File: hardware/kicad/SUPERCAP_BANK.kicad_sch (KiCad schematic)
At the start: 0 parts

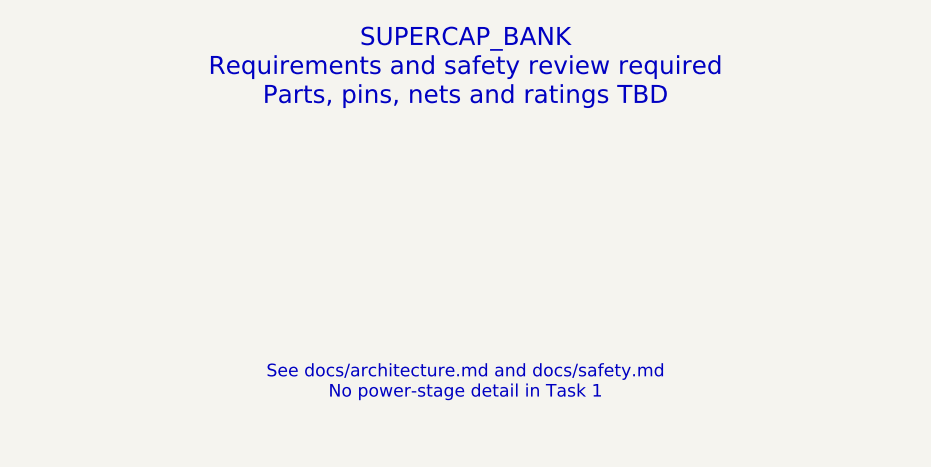
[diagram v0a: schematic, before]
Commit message: hardware: update existing KiCad architecture and add precharge sheet
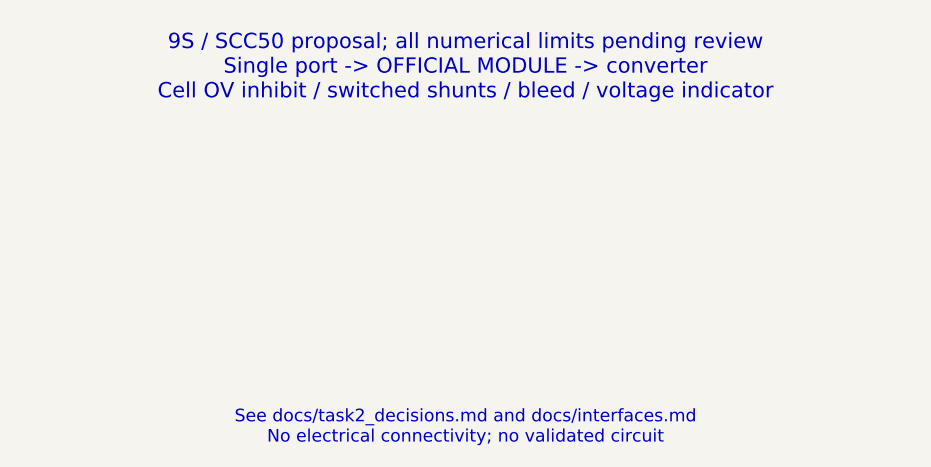
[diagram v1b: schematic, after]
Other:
- note added: "9S / SCC50 proposal; all numerical limits pending review Single port -> OFFICIAL MODULE -> converter Cell OV inhibit / switched shunts / bleed / voltage indicator"
- note added: "See docs/task2_decisions.md and docs/interfaces.md No electrical connectivity; no validated circuit"
- note removed: "SUPERCAP_BANK Requirements and safety review required Parts, pins, nets and ratings TBD"
- note removed: "See docs/architecture.md and docs/safety.md No power-stage detail in Task 1"
- title: SUPERCAP_BANK - Placeholder -> SUPERCAP_BANK - Task 2 Proposal

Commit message: hardware: implement prototype Rev A electrical schematic
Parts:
- added C62, C63, C64, C65, C66, C67, C68, C69, C70: 100nF /50V X7R, Capacitor_SMD:C_0805_2012Metric, symbol RevA:C
- added C71, C72, C73, C74, C75: 100nF / 16V X7R, Capacitor_SMD:C_0805_2012Metric, symbol RevA:C
- added C76: 1uF /50V X7R, Capacitor_SMD:C_0805_2012Metric, symbol RevA:C
- added C77: 470nF /50V X7R, Capacitor_SMD:C_0805_2012Metric, symbol RevA:C
- added C78, C79, C80: 1uF /16V, Capacitor_SMD:C_0805_2012Metric, symbol RevA:C
- added D25: SS110 flyback candidate / release delay MUST VERI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, Diode_SMD:D_SMA, symbol RevA:D
- added F2: ATOF 58V 15A candidate / bidirectional DC interru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, symbol RevA:FUSE
- added J15: 9S bank power -> official module external boundary, symbol RevA:J2
- added J16: CAP_ISO external actuator+feedback, symbol RevA:J4
- added J17: Protected 9S taps / SOURCE-SIDE resistors mandato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, symbol RevA:J10
- added K6: CAP_ISO external NO contact / AEV14012 candidate, symbol RevA:CONTACT
- added Q20: CSD18540Q5B, Package_SON:VSONP-8-1EP_5x6_P1.27mm, symbol RevA:CSD18540Q5B
- added Q21: BC857B, Package_TO_SOT_SMD:SOT-23, symbol RevA:Q_PNP
- added Q22: BC847B, Package_TO_SOT_SMD:SOT-23, symbol RevA:Q_NPN
- added Q23: BC847B preregulator / voltage thermal MUST VERIFY, Package_TO_SOT_SMD:SOT-23, symbol RevA:Q_NPN
- added R122, R123, R124, R128, R139, R140, R141, R142, R143, R145, R146, R150, R151: 10k, Resistor_SMD:R_0805_2012Metric, symbol RevA:R
- added R125: 4.7k, Resistor_SMD:R_0805_2012Metric, symbol RevA:R
- added R126: 100k, Resistor_SMD:R_0805_2012Metric, symbol RevA:R
- added R127: 47R, Resistor_SMD:R_0805_2012Metric, symbol RevA:R
- added R129, R130, R131, R132, R133, R134, R135, R136, R137, R138: 1k /1W tap protection / no bypass, Resistor_SMD:R_2512_6332Metric, symbol RevA:R
- added R144: 100R, Resistor_SMD:R_0805_2012Metric, symbol RevA:R
- added R147, R148, R149: 10k TS commissioning option, Resistor_SMD:R_0805_2012Metric, symbol RevA:R
- added U21: BQ7694204PFBR, Package_QFP:TQFP-48_7x7mm_P0.5mm, symbol RevA:BQ7694204PFBR
- added U22: SN74LV1T34DBVR, Package_TO_SOT_SMD:SOT-23-5, symbol RevA:SN74LV1T34DBVR
- added U23: TPS3839K33DBZR, Package_TO_SOT_SMD:SOT-23, symbol RevA:TPS3839K33DBZR
- added U24: SN74LVC2G08DCUR, Package_SO:VSSOP-8_2.3x2mm_P0.5mm, symbol RevA:SN74LVC2G08DCUR
- added U25, U26: TMUX1511PWR, Package_SO:TSSOP-14_4.4x5mm_P0.65mm, symbol RevA:TMUX1511PWR
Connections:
- new net ACTUATOR_12V: D25.1 (K), J16.1 (P1), K6.3 (COIL_P), Q21.2 (E), R123.2 (B)
- new net BANK_FUSED: F2.2 (B), K6.1 (COM)
- new net BANK_P_RAW: F2.1 (A), J15.1 (P1), J17.10 (P10), R138.1 (A), R144.1 (A), R145.1 (A), R146.1 (A)
- new net CAP_ISOLATED: K6.2 (NO)
- new net CAP_ISO_COIL_GATE: Q20.2 (G_DS4), R122.1 (A), R127.2 (B)
- new net CAP_ISO_COIL_M: D25.2 (A), J16.2 (P2), K6.4 (COIL_M), Q20.3 (D_DS5_6_7_8)
- new net CAP_ISO_DRIVE: R125.1 (A)
- new net CAP_ISO_FB: J16.3 (P3), R128.1 (A)
- new net CAP_ISO_NPN_C: Q22.3 (C), R124.2 (B)
- new net CAP_ISO_NPN_C_BASE: Q22.1 (B), R125.2 (B), R126.1 (A)
- new net CAP_ISO_PNP_B: Q21.1 (B), R123.1 (A), R124.1 (A)
- new net CAP_ISO_PNP_C: Q21.3 (C), R127.1 (A)
- new net CELL0_FILTER: C62.2 (B), R129.2 (B), U21.16 (VC0)
- new net CELL1_FILTER: C62.1 (A), C63.2 (B), R130.2 (B), U21.15 (VC1)
- new net CELL1_RAW: J17.2 (P2), R130.1 (A)
- new net CELL2_FILTER: C63.1 (A), C64.2 (B), R131.2 (B), U21.14 (VC2)
- new net CELL2_RAW: J17.3 (P3), R131.1 (A)
- new net CELL3_FILTER: C64.1 (A), C65.2 (B), R132.2 (B), U21.13 (VC3)
- new net CELL3_RAW: J17.4 (P4), R132.1 (A)
- new net CELL4_FILTER: C65.1 (A), C66.2 (B), R133.2 (B), U21.12 (VC4)
- new net CELL4_RAW: J17.5 (P5), R133.1 (A)
- new net CELL5_FILTER: C66.1 (A), C67.2 (B), R134.2 (B), U21.10 (VC5)
- new net CELL5_RAW: J17.6 (P6), R134.1 (A)
- new net CELL6_FILTER: C67.1 (A), C68.2 (B), R135.2 (B), U21.8 (VC6)
- new net CELL6_RAW: J17.7 (P7), R135.1 (A)
- new net CELL7_FILTER: C68.1 (A), C69.2 (B), R136.2 (B), U21.6 (VC7)
- new net CELL7_RAW: J17.8 (P8), R136.1 (A)
- new net CELL8_FILTER: C69.1 (A), C70.2 (B), R137.2 (B), U21.2 (VC9), U21.4 (VC8)
- new net CELL8_RAW: J17.9 (P9), R137.1 (A)
- new net CELL9_FILTER: C70.1 (A), R138.2 (B), U21.48 (VC10)
- new net GND: C71.2 (B), C72.2 (B), C73.2 (B), C74.2 (B), C75.2 (B), C76.2 (B), C78.2 (B), C79.2 (B), C80.2 (B), J15.2 (P2), J16.4 (P4), J17.1 (P1), Q20.1 (S_DS1_2_3), Q22.2 (E), R122.2 (B), R126.2 (B), R129.1 (A), R139.2 (B), R142.2 (B), R143.2 (B), R147.2 (B), R148.2 (B), R149.2 (B), R150.2 (B), R151.2 (B), U21.17 (VSS), U21.18 (SRP), U21.20 (SRN), U21.30 (DFETOFF), U21.33 (RST_SHUT), U22.3 (GND), U23.1 (GND), U24.4 (GND), U24.5 (A2), U24.6 (B2), U25.7 (GND), U26.12 (S4), U26.5 (S2), U26.7 (GND), U26.9 (S3)
- new net MON_ALERT: R140.1 (A), U21.25 (ALERT), U26.2 (S1)
- new net MON_ALERT_HOST: U26.3 (D1)
- new net MON_BAT: C76.1 (A), C77.2 (B), Q23.3 (C), R144.2 (B), U21.47 (BAT)
- new net MON_BREG: Q23.1 (B), U21.37 (BREG)
- new net MON_COMM_PERMIT: U24.7 (Y1), U25.1 (SEL1), U25.10 (SEL3), U25.13 (SEL4), U25.4 (SEL2), U26.1 (SEL1), U26.10 (SEL3), U26.13 (SEL4), U26.4 (SEL2)
- new net MON_CP: C77.1 (A), U21.46 (CP1)
- new net MON_CS: R141.1 (A), U21.29 (CS_N), U25.8 (D3)
- new net MON_CS_HOST: U25.9 (S3)
- new net MON_DCHG: R150.1 (A), U21.31 (DCHG)
- new net MON_DDSG: R151.1 (A), U21.32 (DDSG)
- new net MON_LD: R146.2 (B), U21.41 (LD)
- new net MON_MISO: R139.1 (A), U21.27 (MISO), U22.2 (A)
- new net MON_MISO_HOST: U25.11 (D4)
- new net MON_MISO_SHIFTED: U22.4 (Y), U25.12 (S4)
- new net MON_MOSI: R143.1 (A), U21.28 (MOSI), U25.6 (D2)
- new net MON_MOSI_HOST: U25.5 (S2)
- new net MON_PACK: R145.2 (B), U21.42 (PACK)
- new net MON_POWER_OK: U23.2 (RESET_N), U24.2 (B1)
- new net MON_REG1: C71.1 (A), C72.1 (A), C79.1 (A), R140.2 (B), R141.2 (B), U21.35 (REG1), U22.5 (VCC), U23.3 (VDD)
- new net MON_REG18: C80.1 (A), U21.24 (REG18)
- new net MON_REGIN: C78.1 (A), Q23.2 (E), U21.36 (REGIN)
- new net MON_SCLK: R142.1 (A), U21.26 (SCLK), U25.3 (D1)
- new net MON_SCLK_HOST: U25.2 (S1)
- new net MON_TS1: R147.1 (A), U21.21 (TS1)
- new net MON_TS2: R148.1 (A), U21.22 (TS2)
- new net MON_TS3: R149.1 (A), U21.23 (TS3)
- new net RAIL_OK: U24.1 (A1)
- new net V3V3: C73.1 (A), C74.1 (A), C75.1 (A), R128.2 (B), U24.8 (VCC), U25.14 (VDD), U26.14 (VDD)
- no-connect marks 0 -> 19
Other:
- note added: "BQ battery-ground SPI is not galvanically isolated; partial-power/backfeed review still mandatory."
- note added: "BQ7694204 SPI/CRC +3.3V REG1 variant. 9S mask: cells1..8 +cell10, VC9 tied to VC8, unused cell9 disabled."
- note added: "DCHG/DDSG configured ACTIVE-HIGH permission, pull-down, protection mapping/readback+power-cycle test mandatory."
- note added: "Internal switched passive balance limited by1k input R; charge must taper/inhibit if balancing cannot keep up."
- note added: "Open-wire current/settling plus input R must be validated; harness source protection before connector is mandatory."
- note added: "Standalone COV/CUV/protection need verified provisioning; defaults for Li-ion are NOT supercap settings."
- note added: "TMUX SPI/ALERT disconnect if either MCU or REG1 power missing; LV1T34 handles initial1.8V MISO level."
- note removed: "9S / SCC50 proposal; all numerical limits pending review Single port -> OFFICIAL MODULE -> converter Cell OV inhibit / switched shunts / bleed / voltage indicator"
- note removed: "See docs/task2_decisions.md and docs/interfaces.md No electrical connectivity; no validated circuit"
- title: SUPERCAP_BANK - Task 2 Proposal -> SUPERCAP_BANK / Prototype Rev A draft

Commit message: hardware: refine Rev A protection and passive selections
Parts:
- removed C62, C63, C64, C65, C66, C67, C68, C69, C70: 100nF /50V X7R, Capacitor_SMD:C_0805_2012Metric, symbol RevA:C
- removed C71: 100nF / 16V X7R, Capacitor_SMD:C_0805_2012Metric, symbol RevA:C
- removed D25: SS110 flyback candidate / release delay MUST VERI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, Diode_SMD:D_SMA, symbol RevA:D
- removed F2: ATOF 58V 15A candidate / bidirectional DC interru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, symbol RevA:FUSE
- removed J15: 9S bank power -> official module external boundary, symbol RevA:J2
- removed J16: CAP_ISO external actuator+feedback, symbol RevA:J4
- removed J17: Protected 9S taps / SOURCE-SIDE resistors mandato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, symbol RevA:J10
- removed K6: CAP_ISO external NO contact / AEV14012 candidate, symbol RevA:CONTACT
- removed Q20: CSD18540Q5B, Package_SON:VSONP-8-1EP_5x6_P1.27mm, symbol RevA:CSD18540Q5B
- removed Q21: BC857B, Package_TO_SOT_SMD:SOT-23, symbol RevA:Q_PNP
- removed Q22: BC847B, Package_TO_SOT_SMD:SOT-23, symbol RevA:Q_NPN
- removed Q23: BC847B preregulator / voltage thermal MUST VERIFY, Package_TO_SOT_SMD:SOT-23, symbol RevA:Q_NPN
- removed U21: BQ7694204PFBR, Package_QFP:TQFP-48_7x7mm_P0.5mm, symbol RevA:BQ7694204PFBR
- removed U22: SN74LV1T34DBVR, Package_TO_SOT_SMD:SOT-23-5, symbol RevA:SN74LV1T34DBVR
- removed U23: TPS3839K33DBZR, Package_TO_SOT_SMD:SOT-23, symbol RevA:TPS3839K33DBZR
- removed U24: SN74LVC2G08DCUR, Package_SO:VSSOP-8_2.3x2mm_P0.5mm, symbol RevA:SN74LVC2G08DCUR
- added C81, C82, C83, C84, C85, C86, C87, C88, C89: 100nF /50V X7R, Capacitor_SMD:C_0805_2012Metric, symbol RevA:C
- added C90, C91, C92, C93, C94: 100nF / 16V X7R, Capacitor_SMD:C_0805_2012Metric, symbol RevA:C
- added C95: 1uF /50V X7R, Capacitor_SMD:C_0805_2012Metric, symbol RevA:C
- added C96, C97, C98: 1uF /16V, Capacitor_SMD:C_0805_2012Metric, symbol RevA:C
- added D23: SMBJ18CA bidirectional coil suppression / release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, Diode_SMD:D_SMB, symbol RevA:D
- added F3: 0997015.WXN / MINI997 58V15A / external 0FHM0002Z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, symbol RevA:FUSE
- added J12: 9S bank power -> official module external boundary, symbol RevA:J2
- added J13: CAP_ISO actuator+reserved diagnostic / no intrins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, symbol RevA:J4
- added J14: Protected 9S taps / source resistors at electrode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, symbol RevA:J10
- added K4: CAP_ISO external NO contact / AEV14012 bench sele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, symbol RevA:CONTACT
- added Q16: CSD18540Q5B, Package_SON:VSONP-8-1EP_5x6_P1.27mm, symbol RevA:CSD18540Q5B
- added Q17: BC857B, Package_TO_SOT_SMD:SOT-23, symbol RevA:Q_PNP
- added Q18: BC847B, Package_TO_SOT_SMD:SOT-23, symbol RevA:Q_NPN
- added Q19: BC847B preregulator / voltage thermal MUST VERIFY, Package_TO_SOT_SMD:SOT-23, symbol RevA:Q_NPN
- added R116, R117, R118, R155, R156: 10k, Resistor_SMD:R_0805_2012Metric, symbol RevA:R
- added R119: 4.7k, Resistor_SMD:R_0805_2012Metric, symbol RevA:R
- added R120: 100k, Resistor_SMD:R_0805_2012Metric, symbol RevA:R
- added R121: 47R, Resistor_SMD:R_0805_2012Metric, symbol RevA:R
- added R152, R153, R154: 10k TS commissioning option, Resistor_SMD:R_0805_2012Metric, symbol RevA:R
- added U27: SN74LV1T34DBVR, Package_TO_SOT_SMD:SOT-23-5, symbol RevA:SN74LV1T34DBVR
- added U28: TPS3839K33DBZR, Package_TO_SOT_SMD:SOT-23, symbol RevA:TPS3839K33DBZR
- added U29: SN74LVC2G08DCUR, Package_SO:VSSOP-8_2.3x2mm_P0.5mm, symbol RevA:SN74LVC2G08DCUR
- added U30, U31: TMUX1511PWR, Package_SO:TSSOP-14_4.4x5mm_P0.65mm, symbol RevA:TMUX1511PWR
- C72, C73, C74, C75: value 100nF / 16V X7R -> 50F /2.7V SCCV40B506SRB / external cell; footprint Capacitor_SMD:C_0805_2012Metric -> (none); MPN (none) -> SCCV40B506SRB
- C76: value 1uF /50V X7R -> 50F /2.7V SCCV40B506SRB / external cell; footprint Capacitor_SMD:C_0805_2012Metric -> (none); MPN (none) -> SCCV40B506SRB
- C77: value 470nF /50V X7R -> 50F /2.7V SCCV40B506SRB / external cell; footprint Capacitor_SMD:C_0805_2012Metric -> (none); MPN (none) -> SCCV40B506SRB
- C78, C79, C80: value 1uF /16V -> 50F /2.7V SCCV40B506SRB / external cell; footprint Capacitor_SMD:C_0805_2012Metric -> (none); MPN (none) -> SCCV40B506SRB
- R122, R143, R145, R146, R150, R151: MPN (none) -> CRCW080510K0FKEA
- R123, R124, R128: value 10k -> 1k /1W EXTERNAL cell-terminal tap resistor; footprint Resistor_SMD:R_0805_2012Metric -> (none); MPN (none) -> CRCW25121K00FKEG
- R125: value 4.7k -> 1k /1W EXTERNAL cell-terminal tap resistor; footprint Resistor_SMD:R_0805_2012Metric -> (none); MPN (none) -> CRCW25121K00FKEG
- R126: value 100k -> 1k /1W EXTERNAL cell-terminal tap resistor; footprint Resistor_SMD:R_0805_2012Metric -> (none); MPN (none) -> CRCW25121K00FKEG
- R127: value 47R -> 1k /1W EXTERNAL cell-terminal tap resistor; footprint Resistor_SMD:R_0805_2012Metric -> (none); MPN (none) -> CRCW25121K00FKEG
- R129, R130, R131, R132: value 1k /1W tap protection / no bypass -> 1k /1W EXTERNAL cell-terminal tap resistor; footprint Resistor_SMD:R_2512_6332Metric -> (none); MPN (none) -> CRCW25121K00FKEG
- R133, R134, R135, R136, R137, R138: MPN (none) -> CRCW25121K00FKEG
- R139, R140, R141, R142: value 10k -> 1k /1W tap protection / no bypass; footprint Resistor_SMD:R_0805_2012Metric -> Resistor_SMD:R_2512_6332Metric; MPN (none) -> CRCW25121K00FKEG
- R144: value 100R -> 10k; MPN (none) -> CRCW080510K0FKEA
- R147: value 10k TS commissioning option -> 10k; MPN (none) -> CRCW080510K0FKEA
- R148: value 10k TS commissioning option -> 100R; MPN (none) -> CRCW0805100RFKEA
- R149: value 10k TS commissioning option -> 0R; MPN (none) -> CRCW08050000Z0EA
- U25: value TMUX1511PWR -> Blue Sea6006 / external manual bank disconnect;not a fault breaker; footprint Package_SO:TSSOP-14_4.4x5mm_P0.65mm -> (none); symbol RevA:TMUX1511PWR -> RevA:DISCONNECT; MPN (none) -> 6006
- U26: value TMUX1511PWR -> BQ7694204PFBR; footprint Package_SO:TSSOP-14_4.4x5mm_P0.65mm -> Package_QFP:TQFP-48_7x7mm_P0.5mm; symbol RevA:TMUX1511PWR -> RevA:BQ7694204PFBR; MPN (none) -> BQ7694204PFBR
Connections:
- net ACTUATOR_12V: now also D23.1 (K), J13.1 (P1), K4.3 (COIL_P), Q17.2 (E), R117.2 (B); no longer R123.2 (B)
- net BANK_FUSED: now also F3.2 (B), K4.1 (COM)
- net BANK_P_RAW: now also C80.1 (A), R132.1 (A), R148.1 (A), R150.1 (A), R151.1 (A), U25.1 (COM), J12.1 (P1); no longer R138.1 (A), R144.1 (A), R145.1 (A), R146.1 (A)
- net CAP_ISOLATED: now also K4.2 (NO)
- net CAP_ISO_COIL_GATE: now also Q16.2 (G_DS4), R116.1 (A), R121.2 (B); no longer R122.1 (A), R127.2 (B)
- net CAP_ISO_COIL_M: now also D23.2 (A), J13.2 (P2), K4.4 (COIL_M), Q16.3 (D_DS5_6_7_8)
- net CAP_ISO_DRIVE: now also R119.1 (A); no longer R125.1 (A)
- net CAP_ISO_FB: now also R122.1 (A), J13.3 (P3); no longer R128.1 (A)
- net CAP_ISO_NPN_C: now also Q18.3 (C), R118.2 (B); no longer R124.2 (B)
- net CAP_ISO_NPN_C_BASE: now also Q18.1 (B), R119.2 (B), R120.1 (A); no longer R125.2 (B), R126.1 (A)
- net CAP_ISO_PNP_B: now also Q17.1 (B), R117.1 (A), R118.1 (A); no longer R123.1 (A), R124.1 (A)
- net CAP_ISO_PNP_C: now also Q17.3 (C), R121.1 (A); no longer R127.1 (A)
- net CELL0_FILTER: now also R133.2 (B), U26.16 (VC0), C81.2 (B); no longer R129.2 (B)
- net CELL1_FILTER: now also R134.2 (B), U26.15 (VC1), C81.1 (A), C82.2 (B); no longer R130.2 (B)
- net CELL1_RAW: now also C72.1 (A), C73.2 (B), R124.1 (A); no longer R130.1 (A)
- net CELL2_FILTER: now also R135.2 (B), U26.14 (VC2), C82.1 (A), C83.2 (B); no longer R131.2 (B)
- net CELL2_RAW: now also C73.1 (A), C74.2 (B), R125.1 (A); no longer R131.1 (A)
- net CELL3_FILTER: now also R136.2 (B), U26.13 (VC3), C83.1 (A), C84.2 (B); no longer R132.2 (B)
- net CELL3_RAW: now also C74.1 (A), C75.2 (B), R126.1 (A); no longer R132.1 (A)
- net CELL4_FILTER: now also R137.2 (B), U26.12 (VC4), C84.1 (A), C85.2 (B); no longer R133.2 (B)
- net CELL4_RAW: now also C75.1 (A), C76.2 (B), R127.1 (A); no longer R133.1 (A)
- net CELL5_FILTER: now also R138.2 (B), U26.10 (VC5), C85.1 (A), C86.2 (B); no longer R134.2 (B)
- net CELL5_RAW: now also C76.1 (A), C77.2 (B), R128.1 (A); no longer R134.1 (A)
- net CELL6_FILTER: now also R139.2 (B), U26.8 (VC6), C86.1 (A), C87.2 (B); no longer R135.2 (B)
- net CELL6_RAW: now also C77.1 (A), C78.2 (B), R129.1 (A); no longer R135.1 (A)
- net CELL7_FILTER: now also R140.2 (B), U26.6 (VC7), C87.1 (A), C88.2 (B); no longer R136.2 (B)
- net CELL7_RAW: now also C78.1 (A), C79.2 (B), R130.1 (A); no longer R136.1 (A)
- net CELL8_FILTER: now also R141.2 (B), U26.2 (VC9), U26.4 (VC8), C88.1 (A), C89.2 (B); no longer R137.2 (B)
- net CELL8_RAW: now also C79.1 (A), C80.2 (B), R131.1 (A); no longer R137.1 (A)
- net CELL9_FILTER: now also R142.2 (B), U26.48 (VC10), C89.1 (A); no longer R138.2 (B)
- net GND: now also R123.1 (A), R146.2 (B), U26.17 (VSS), U26.18 (SRP), U26.20 (SRN), U26.30 (DFETOFF), U26.33 (RST_SHUT), C90.2 (B), C91.2 (B), C92.2 (B), C93.2 (B), C94.2 (B), C95.2 (B), C96.2 (B), C97.2 (B), C98.2 (B), J12.2 (P2), J13.4 (P4), Q16.1 (S_DS1_2_3), Q18.2 (E), R116.2 (B), R120.2 (B), R152.2 (B), R153.2 (B), R154.2 (B), R155.2 (B), R156.2 (B), U27.3 (GND), U28.1 (GND), U29.4 (GND), U29.5 (A2), U29.6 (B2), U30.7 (GND), U31.12 (S4), U31.5 (S2), U31.7 (GND), U31.9 (S3); no longer C73.2 (B), C74.2 (B), C75.2 (B), C76.2 (B), C78.2 (B), C79.2 (B), C80.2 (B), R126.2 (B), R129.1 (A), R139.2 (B), R142.2 (B), R148.2 (B), R149.2 (B), R150.2 (B), R151.2 (B), U25.7 (GND), U26.12 (S4), U26.5 (S2), U26.7 (GND), U26.9 (S3)
- net MON_ALERT: now also R144.1 (A), U26.25 (ALERT), U31.2 (S1); no longer R140.1 (A), U26.2 (S1)
- net MON_ALERT_HOST: now also U31.3 (D1); no longer U26.3 (D1)
- net MON_BAT: now also R148.2 (B), R149.2 (B), U26.47 (BAT), C95.1 (A), Q19.3 (C); no longer C76.1 (A), C77.2 (B), R144.2 (B)
- net MON_BREG: now also U26.37 (BREG), Q19.1 (B)
- net MON_COMM_PERMIT: now also U29.7 (Y1), U30.1 (SEL1), U30.10 (SEL3), U30.13 (SEL4), U30.4 (SEL2), U31.1 (SEL1), U31.10 (SEL3), U31.13 (SEL4), U31.4 (SEL2); no longer U25.1 (SEL1), U25.10 (SEL3), U25.13 (SEL4), U25.4 (SEL2), U26.1 (SEL1), U26.10 (SEL3), U26.13 (SEL4), U26.4 (SEL2)
- net MON_CP: now also R149.1 (A), U26.46 (CP1); no longer C77.1 (A)
- net MON_CS: now also R145.1 (A), U26.29 (CS_N), U30.8 (D3); no longer R141.1 (A), U25.8 (D3)
- net MON_CS_HOST: now also U30.9 (S3); no longer U25.9 (S3)
- net MON_DCHG: now also U26.31 (DCHG), R155.1 (A); no longer R150.1 (A)
- net MON_DDSG: now also U26.32 (DDSG), R156.1 (A); no longer R151.1 (A)
- net MON_LD: now also R151.2 (B), U26.41 (LD); no longer R146.2 (B)
- net MON_MISO: now also R143.1 (A), U26.27 (MISO), U27.2 (A); no longer R139.1 (A)
- net MON_MISO_HOST: now also U30.11 (D4); no longer U25.11 (D4)
- net MON_MISO_SHIFTED: now also U27.4 (Y), U30.12 (S4); no longer U25.12 (S4)
- net MON_MOSI: now also R147.1 (A), U26.28 (MOSI), U30.6 (D2); no longer R143.1 (A), U25.6 (D2)
- net MON_MOSI_HOST: now also U30.5 (S2); no longer U25.5 (S2)
- net MON_PACK: now also R150.2 (B), U26.42 (PACK); no longer R145.2 (B)
- net MON_POWER_OK: now also U28.2 (RESET_N), U29.2 (B1)
- net MON_REG1: now also R144.2 (B), R145.2 (B), U26.35 (REG1), C90.1 (A), C91.1 (A), C97.1 (A), U27.5 (VCC), U28.3 (VDD); no longer C72.1 (A), C79.1 (A), R140.2 (B), R141.2 (B)
- net MON_REG18: now also U26.24 (REG18), C98.1 (A); no longer C80.1 (A)
- net MON_REGIN: now also U26.36 (REGIN), C96.1 (A), Q19.2 (E); no longer C78.1 (A)
- net MON_SCLK: now also R146.1 (A), U26.26 (SCLK), U30.3 (D1); no longer R142.1 (A), U25.3 (D1)
- net MON_SCLK_HOST: now also U30.2 (S1); no longer U25.2 (S1)
- net MON_TS1: now also U26.21 (TS1), R152.1 (A); no longer R147.1 (A)
- net MON_TS2: now also U26.22 (TS2), R153.1 (A); no longer R148.1 (A)
- net MON_TS3: now also U26.23 (TS3), R154.1 (A); no longer R149.1 (A)
- net RAIL_OK: now also U29.1 (A1)
- net V3V3: now also C92.1 (A), C93.1 (A), C94.1 (A), U29.8 (VCC), U30.14 (VDD), U31.14 (VDD); no longer C73.1 (A), C74.1 (A), C75.1 (A), R128.2 (B), U25.14 (VDD), U26.14 (VDD)
- new net BANK_MANUAL_OUT: F3.1 (A), U25.2 (SWITCHED)
- new net TAP0_SOURCE_PROTECTED: J14.1 (P1), R123.2 (B), R133.1 (A)
- new net TAP1_SOURCE_PROTECTED: J14.2 (P2), R124.2 (B), R134.1 (A)
- new net TAP2_SOURCE_PROTECTED: J14.3 (P3), R125.2 (B), R135.1 (A)
- new net TAP3_SOURCE_PROTECTED: J14.4 (P4), R126.2 (B), R136.1 (A)
- new net TAP4_SOURCE_PROTECTED: J14.5 (P5), R127.2 (B), R137.1 (A)
- new net TAP5_SOURCE_PROTECTED: J14.6 (P6), R128.2 (B), R138.1 (A)
- new net TAP6_SOURCE_PROTECTED: J14.7 (P7), R129.2 (B), R139.1 (A)
- new net TAP7_SOURCE_PROTECTED: J14.8 (P8), R130.2 (B), R140.1 (A)
- new net TAP8_SOURCE_PROTECTED: J14.9 (P9), R131.2 (B), R141.1 (A)
- new net TAP9_SOURCE_PROTECTED: J14.10 (P10), R132.2 (B), R142.1 (A)
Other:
- note added: "DCHG/DDSG active-LOW fault / healthy-HIGH REG1 permission,0xA6,pull-down. Never use Li-ion defaults."
- note added: "Host-only balance,2k total input resistance/tap including external1k; slow trim,not full-current balancing."
- note added: "RAM profile firmware/config/bq76942_rev_a.json: COV2.530V, CUV1.2144V, delay~10ms; readback mandatory."
- note removed: "DCHG/DDSG configured ACTIVE-HIGH permission, pull-down, protection mapping/readback+power-cycle test mandatory."
- note removed: "Internal switched passive balance limited by1k input R; charge must taper/inhibit if balancing cannot keep up."
- note removed: "Standalone COV/CUV/protection need verified provisioning; defaults for Li-ion are NOT supercap settings."
- moved on the sheet: C72, C73, C74, C75, C76, C77, C78, C79, C80, R122, R123, R124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
